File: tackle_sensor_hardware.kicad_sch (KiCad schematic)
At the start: 72 parts, among them J1 Conn_01x02_Male, J2 Conn_01x04_Male, J3 Conn_01x03_Male, J4 Conn_ARM_JTAG_SWD_10, Q1 DMP4051LK3, Q9 CSD19538Q3A, SW1 PTS645SL43SMTR92 LFS, SW2 SW_DPDT_x2, T1 DRQ125-330-R, U1 LIS2DE12, U2 STM32G031Fx, U3 LM3488, U4 LD1117S33TR_SOT223, U5 ULN2003ADR

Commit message: updating the BOM
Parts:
- removed C3: 10u, Capacitor_SMD:C_0603_1608Metric, symbol Device:C_Small
- removed R10, R8: 10k,1%,63mW, Resistor_SMD:R_0402_1005Metric, symbol Device:R_US
- removed R15: 1k,1%,25mW, Resistor_SMD:R_0603_1608Metric, symbol Device:R_US
- removed R20, R23: 0,0.5W, Resistor_SMD:R_1210_3225Metric, symbol Device:R_US
- removed R22: 220,1%,63mW, Resistor_SMD:R_0402_1005Metric, symbol Device:R_US
- added C11: 1uF, 50V, Capacitor_SMD:C_0603_1608Metric, symbol Device:C
- added R12, R14: 1k,1%,25mW, Resistor_SMD:R_0603_1608Metric, symbol Device:R_US
- added R17: 0,0.5W, Resistor_SMD:R_1210_3225Metric, symbol Device:R_US
- added R18: 220,1%,63mW, Resistor_SMD:R_0402_1005Metric, symbol Device:R_US
- added R3, R5: 10k,1%,63mW, Resistor_SMD:R_0402_1005Metric, symbol Device:R_US
- C1: Field5 C49678 -> (none); JLCPN (none) -> C49678
- C14: renamed from C11; Field5 C49678 -> (none); JLCPN (none) -> C49678
- C5: renamed from C6; JLCPB C338130 -> (none); JLCPN (none) -> C338130
- D1: renamed from D4; JLCPN (none) -> C188533
- D2: renamed from D1; value SS2PH10HM3_A/H -> DSK34; footprint Diode_SMD:D_Powermite_AK -> Diode_SMD:D_SOD-123F; JLCPN (none) -> C41029; MPN (none) -> DSK34
- Q2: renamed from Q9; value CSD19538Q3A -> NCE0110K; footprint Package_SON:VSON-8_3.3x3.3mm_P0.65mm_NexFET -> Package_TO_SOT_SMD:TO-252-2; JLCPN (none) -> C95272; MPN (none) -> NCE0110K
- R1, R9: JLCPN (none) -> C25744; MPN (none) -> 0402WGF1002TCE
- R10: renamed from R2; JLCPN (none) -> C106231; MPN RMCF0402ZT0R00 -> RC0402FR-070RL
- R11, R13: JLCPN (none) -> C21190; MPN ERJ-PA3F1001V -> 0603WAF1001T5E
- R15: renamed from R18; JLCPN (none) -> C620661; MPN RMCF1210ZT0R00 -> 1210W2F1000T5E
- R16: renamed from R21; JLCPN (none) -> C25091; MPN RC0402FR-07220RL -> 0402WGF2200TCE
- R19: value 1k,1%,25mW -> 0,0.5W; footprint Resistor_SMD:R_0603_1608Metric -> Resistor_SMD:R_1210_3225Metric; JLCPN (none) -> C620661; MPN ERJ-PA3F1001V -> 1210W2F1000T5E
- R2: renamed from R3; value 634,.1%,0.1W -> 634,.1%,63mW; JLCPN (none) -> C2998183; MPN ERJ-2RKF6340X -> FRC0402F6340TS
- R4: JLCPN (none) -> C54968; MPN RC0402FR-0756K2L -> 0402WGF5622TCE
- R6: renamed from R5; JLCPN (none) -> C25076; MPN RC0402FR-07100RL -> 0402WGF1000TCE
- R7: renamed from R6; JLCPN (none) -> C160920; MPN CSR1206FK25L0 -> RL12FTNR200
- R8: renamed from R7; JLCPN (none) -> C100545; MPN RMCF0402FT84K5 -> CR0402FF8452G
- SW1: JLCPN (none) -> C221875; MPN (none) -> PTS645SL43SMTR92LFS
- SW2: footprint (none) -> rfc_footprint_lib:SS-3235S-L3
- SW2: JLCPN (none) -> C381098; MPN (none) -> SS-3235S-L3
- T1: MPN (none) -> DRQ125-330-R
- U1: renamed from U2; JLCPN (none) -> C529334; MPN (none) -> STM32G031F8P6
- renumbered C9 to C10, C10 to C12, C12 to C13, C13 to C15, C4 to C2, C5 to C3, C15 to C4, C7 to C6, C16 to C7, C2 to C9, D2 to D4, J4 to J1, J1 to J2, J2 to J4, TP6 to TP10, TP7 to TP11, TP10 to TP12, TP8 to TP13, TP9 to TP14, TP11 to TP15, TP15 to TP4, TP12 to TP5, TP13 to TP6, TP14 to TP7, TP4 to TP8, TP5 to TP9, U3 to U2, U1 to U3
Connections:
- net +3V3: now also C11.1, R5.1; no longer R9.1
- net GND: now also R9.2, C11.2, R12.2, R3.1; no longer R19.2
- net SWCLK: now also R3.2
- net UART_TX: now also R18.1
- net at R8.2, U2.3 (FB): now also R9.1
- net at U2.6 (DR): now also Q2.1 (G); no longer Q2.4 (G)
- net at Q2.2 (S), Q2.3 (S), R6.2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: no longer Q2.1 (S)
- net at R15.1: now also J4.2 (Pin_2); no longer U5.13 (O4)
- net at R15.2: now also U5.13 (O4); no longer J4.2 (Pin_2)
- net at J3.1 (Pin_1): now also R18.2
- net at SW2.2 (B), SW2.5 (B), U1.3 (PC15-OSC32_OUT): now also R5.2; no longer R9.2
- net at U5.11 (O6): now also R19.2
- net at J4.4 (Pin_4): now also R19.1
- net at D3.1 (K): now also R12.1; no longer R19.1
- net at D4.3 (GK): now also R14.1
- net at U5.14 (O3): now also R14.2
- net at C10.2, T1.2 (AB): now also Q2.2 (S); no longer Q2.5 (D)
- net at J4.3 (Pin_3): now also R17.1
- net at U5.12 (O5): now also R17.2
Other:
- note added: "Mode Selection - Eligible Receiver (HIGH) - Ineligible Receiver (LOW)"
- note added: "Power supply decoupling capacitors should be placed as near as possible to pin 9 of the device."
- note removed: "Mode Selection - Ineligible Receiver (HIGH) - Eligible Receiver (LOW)"
- note removed: "Power supply decoupling capacitors (100 nF ceramic, 10 μF aluminum) should be placed as near as possible to pin 9 of the device."
- moved on the sheet: C1, C14, C4, C7, C9, D4, F1, J1, R10, R11, R15, SW1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

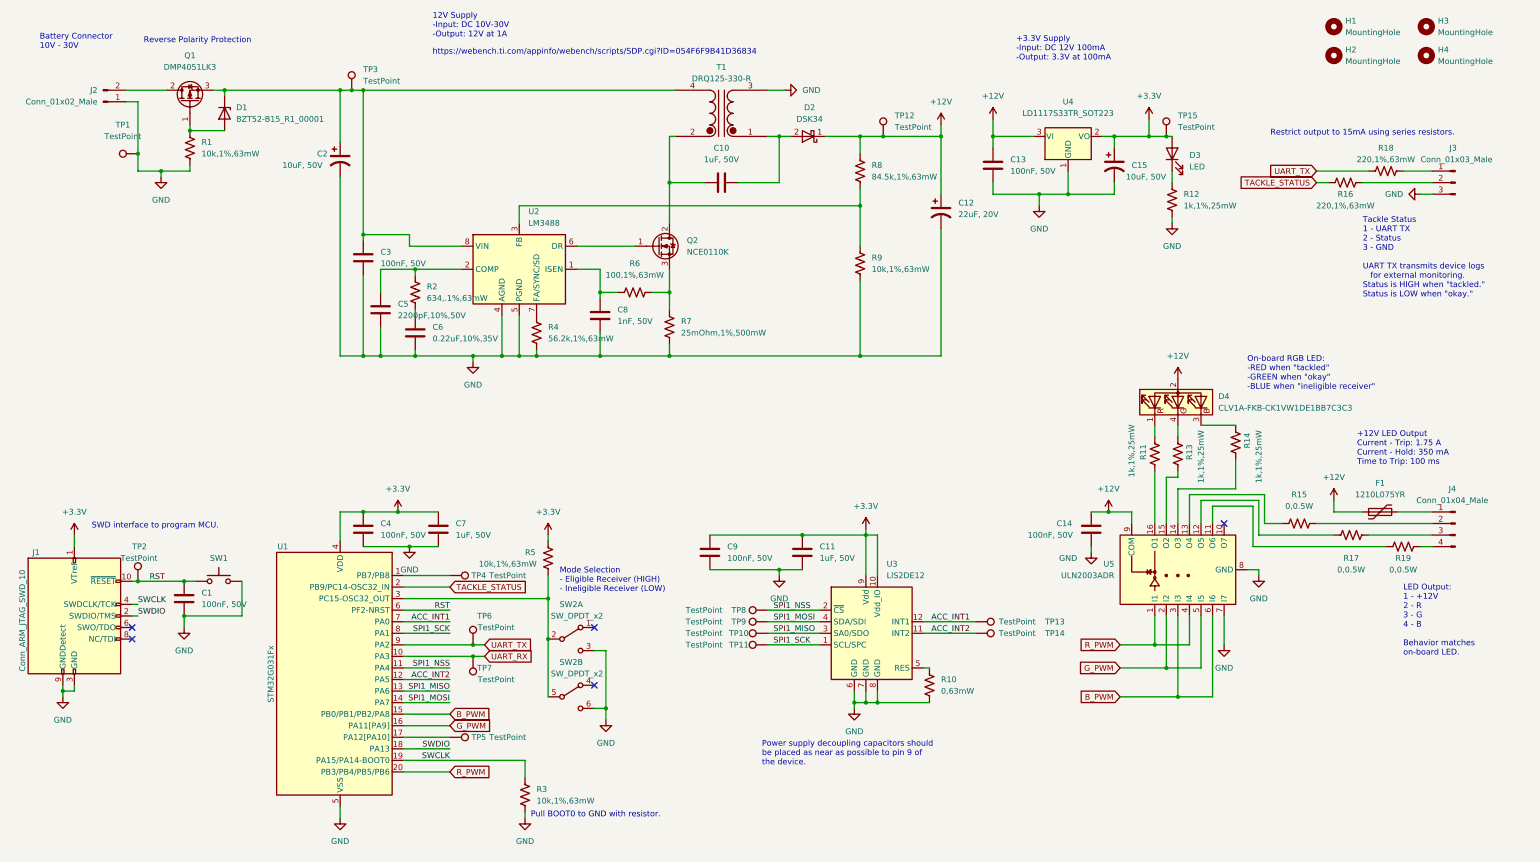
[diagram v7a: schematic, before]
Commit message: rerouted PCB after changes
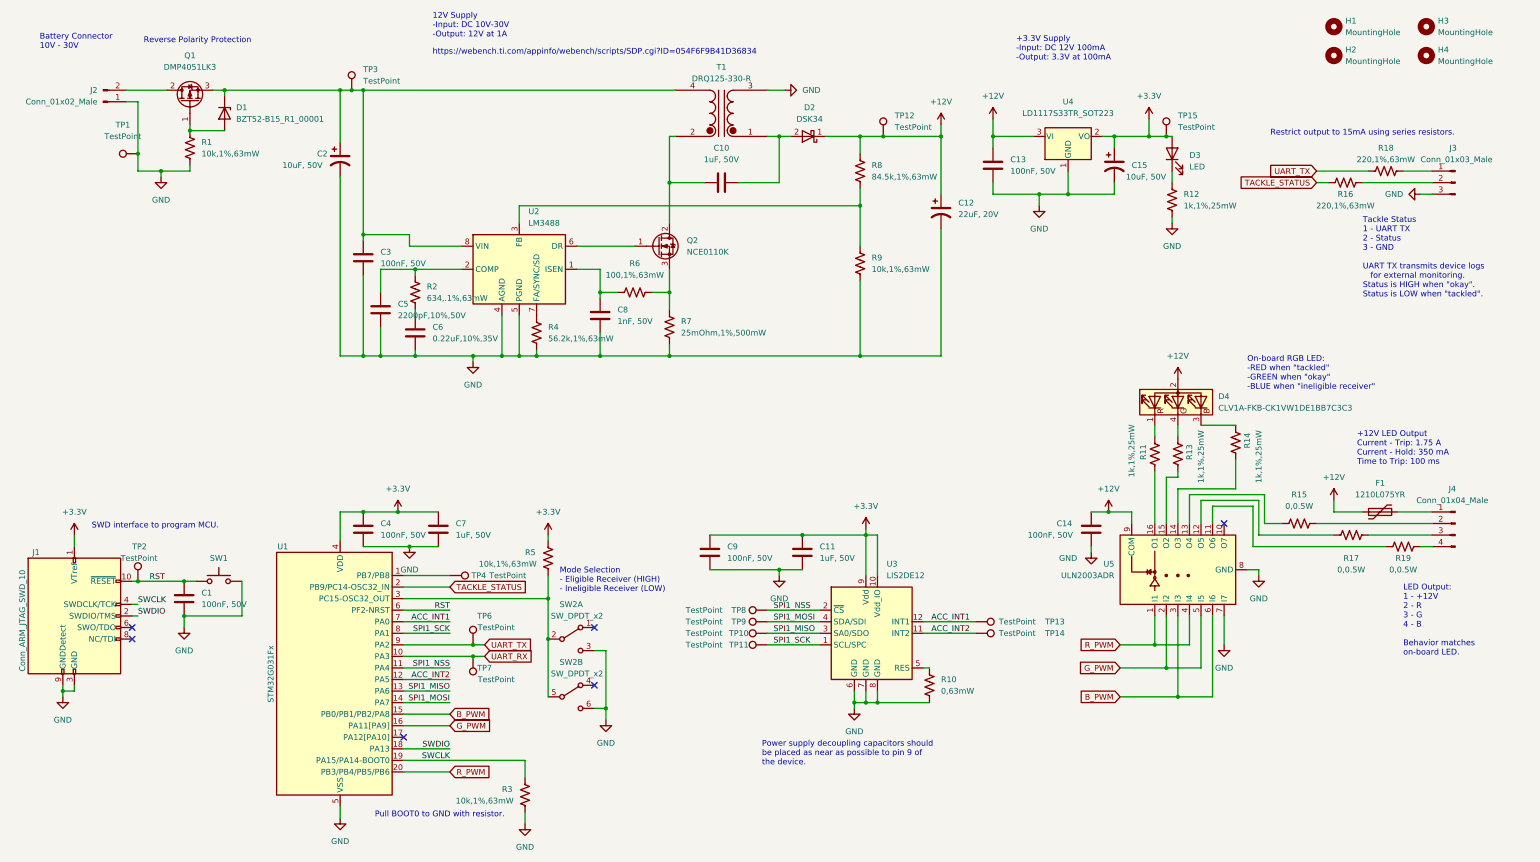
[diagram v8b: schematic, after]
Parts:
- removed TP5: TestPoint, TestPoint:TestPoint_Pad_D1.0mm, symbol Connector:TestPoint
- TP1, TP12, TP15, TP3: footprint TestPoint:TestPoint_Pad_D1.5mm -> TestPoint:TestPoint_Pad_D1.0mm
- TP10, TP11, TP13, TP14, TP6, TP8, TP9: footprint TestPoint:TestPoint_Pad_D1.0mm -> rfc_footprint_lib:test_point
- TP2: footprint TestPoint:TestPoint_Pad_D1.5mm -> rfc_footprint_lib:test_point
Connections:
- no-connect marks 5 -> 6
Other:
- note added: "Tackle Status 1 - UART TX 2 - Status 3 - GND UART TX transmits device logs for external monitoring. Status is HIGH when "okay". Status is LOW when "tackled"."
- note removed: "Tackle Status 1 - UART TX 2 - Status 3 - GND UART TX transmits device logs for external monitoring. Status is HIGH when "tackled." Status is LOW when "okay.""
